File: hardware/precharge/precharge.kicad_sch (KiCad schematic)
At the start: 7 parts

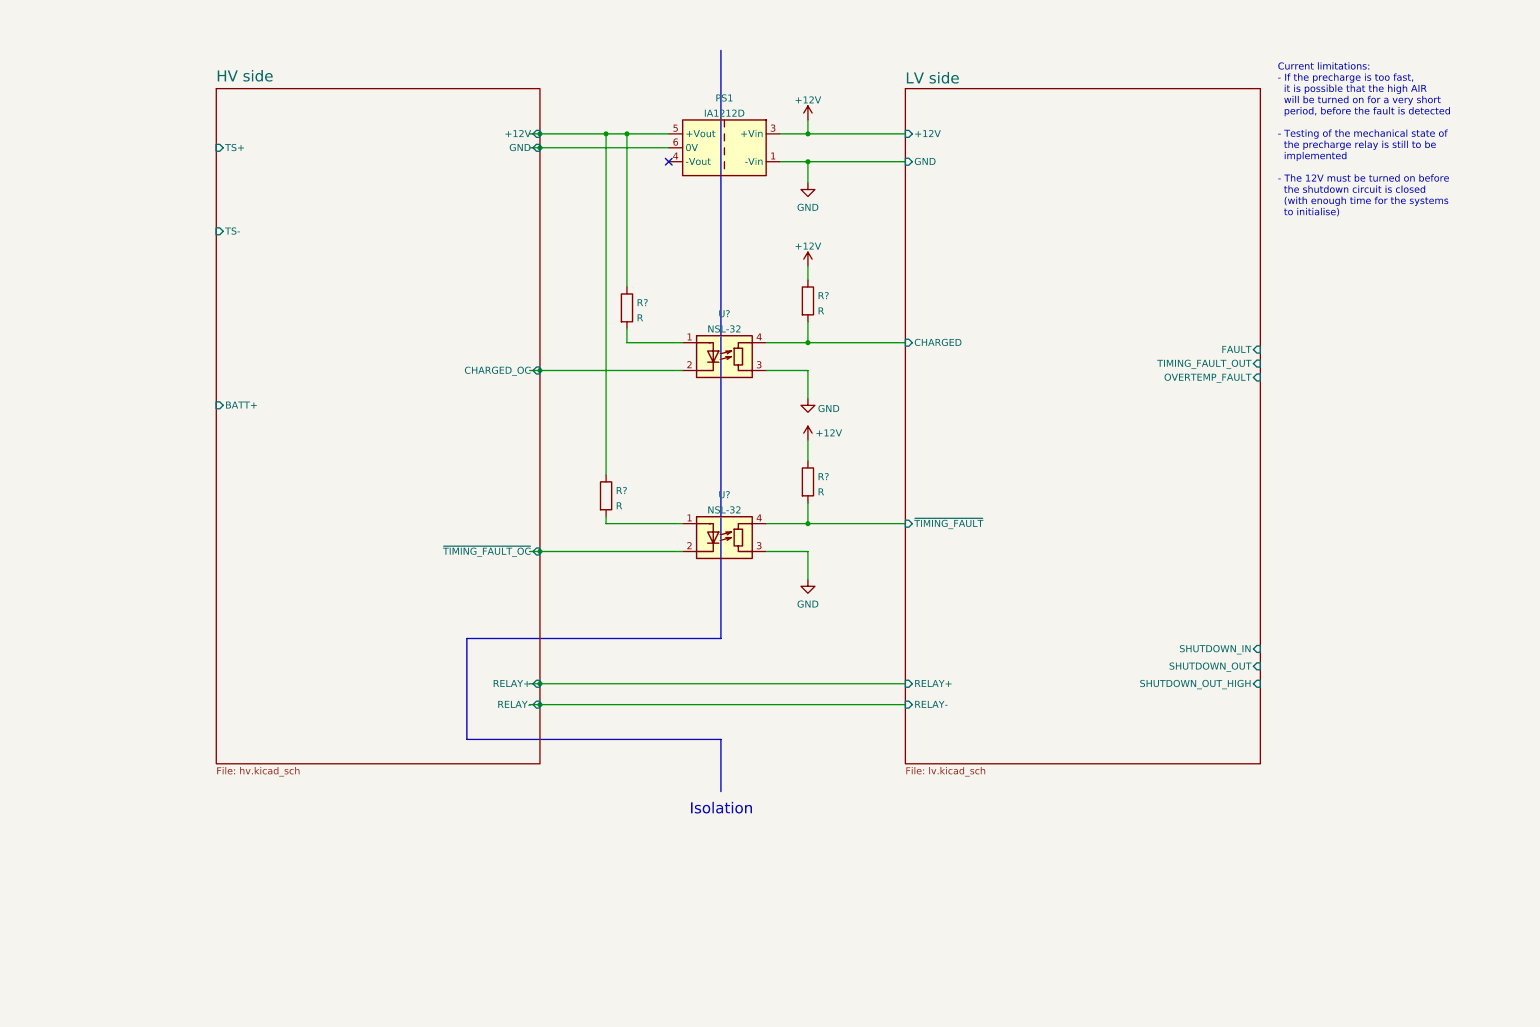
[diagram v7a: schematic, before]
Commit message: Updated quite a bit
- Added relay mechanical state detection

- Selected most component values for HV side

- Other miscellaneous changes
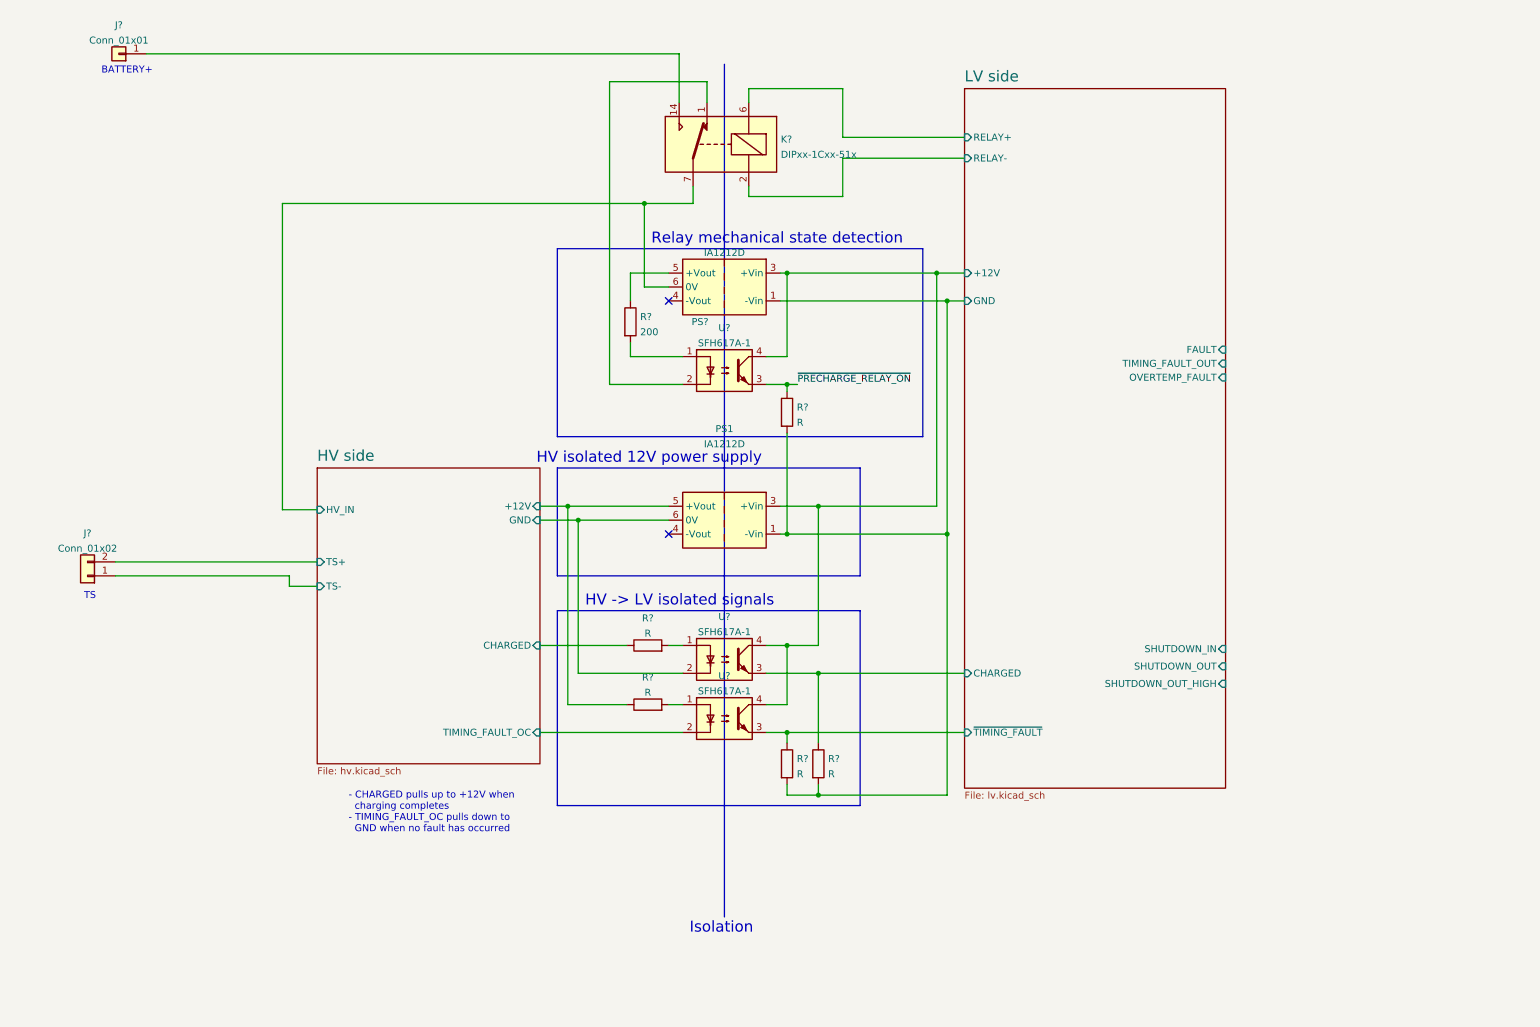
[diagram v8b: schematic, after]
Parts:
- removed U? (x2): NSL-32, OptoDevice:Luna_NSL-32, symbol Isolator:NSL-32
- added J?: Conn_01x01, symbol Connector_Generic:Conn_01x01
- added J?: Conn_01x02, symbol Connector_Generic:Conn_01x02
- added K?: DIPxx-1Cxx-51x, Relay_THT:Relay_StandexMeder_DIP_LowProfile, symbol Relay:DIPxx-1Cxx-51x
- added PS?: IA1212D, Converter_DCDC:Converter_DCDC_XP_POWER-IAxxxxD_THT, symbol Converter_DCDC:IA1212D
- added R?: 200, symbol Device:R
- added R?: R, symbol Device:R
- added U? (x3): SFH617A-1, Package_DIP:DIP-4_W7.62mm, symbol Isolator:SFH617A-1
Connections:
- net HV side/+12V: no longer R?.1
- net HV side/GND: now also U?.2
- net HV side/TS+: now also J?.2 (Pin_2)
- net HV side/TS-: now also J?.1 (Pin_1)
- net LV side/CHARGED: now also R?.1, U?.3; no longer R?.2
- net LV side/~{TIMING_FAULT}: now also R?.1, U?.3; no longer R?.2
- net at R?.2: now also U?.1 (x2)
- removed net +12V: PS1.3 (+Vin), R?.1, R?.1
- net GND renamed LV side/GND
- net LV side/GND: now also R?.2, R?.2, PS?.1 (-Vin), R?.2
- new net: PS?.5 (+Vout), R?.1
- new net: R?.2, U?.1
- new net: J?.1 (Pin_1), K?.14
- new net: K?.1, U?.2
- new net HV side/CHARGED: R?.1
- new net HV side/HV_IN: K?.7, K?.8, PS?.6 (0V)
- new net HV side/TIMING_FAULT_OC: U?.2
- new net LV side/+12V: PS1.3 (+Vin), PS?.3 (+Vin), U?.4, U?.4, U?.4
- new net LV side/RELAY+: K?.6
- new net LV side/RELAY-: K?.2
- new net ~{PRECHARGE_RELAY_ON}: R?.1, U?.3
- no-connect marks 1 -> 2
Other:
- sheet HV side ports: added CHARGED, HV_IN, TIMING_FAULT_OC; removed BATT+, CHARGED_OC, RELAY+, RELAY-, ~{TIMING_FAULT_OC}
- note added: "- CHARGED pulls up to +12V when charging completes - TIMING_FAULT_OC pulls down to GND when no fault has occurred"
- note added: "BATTERY+"
- note added: "HV -> LV isolated signals"
- note added: "HV isolated 12V power supply"
- note added: "Relay mechanical state detection"
- note added: "TS"
- note removed: "Current limitations: - If the precharge is too fast, it is possible that the high AIR will be turned on for a very short period, before the fault is detected - Testing of the mechanical state of the precharge relay is still to be implemented - The 12V must be turned on before the shutdown circuit is closed (with enough time for the systems to initialise)"
- moved on the sheet: PS1, R?
